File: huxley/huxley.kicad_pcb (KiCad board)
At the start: 4 copper layers, 104 parts, among them J1 SMA_RF2-04A-T-00-50-G, J10 SMA_RF2-04A-T-00-50-G, J11 SMA_RF2-04A-T-00-50-G, J12 SMA_RF2-04A-T-00-50-G, J13 SMA_RF2-04A-T-00-50-G, J14 SMA_RF2-04A-T-00-50-G, J15 SMA_RF2-04A-T-00-50-G, J16 SMA_RF2-04A-T-00-50-G, J17 SMA_RF2-04A-T-00-50-G, J18 SMA_RF2-04A-T-00-50-G, J19 SMA_RF2-04A-T-00-50-G, J2 SMA_RF2-04A-T-00-50-G, J20 SMA_RF2-04A-T-00-50-G, J21 61300211121, J22 SMA_RF2-04A-T-00-50-G, J23 SMA_RF2-04A-T-00-50-G, J24 SMA_RF2-04A-T-00-50-G, J25 61300211121, J26 61300211121, J27 61300211121, J28 61300211121, J29 61300211121, J3 SMA_RF2-04A-T-00-50-G, J30 61300211121, J31 61300211121, J32 61300211121, J33 67996-130HLF, J4 SMA_RF2-04A-T-00-50-G, J5 SMA_RF2-04A-T-00-50-G, J6 SMA_RF2-04A-T-00-50-G, J7 SMA_RF2-04A-T-00-50-G, J8 SMA_RF2-04A-T-00-50-G, J9 SMA_RF2-04A-T-00-50-G, U2 LM134H, U3 MAX40201FAUA+, U4 TMUX1112PWR, U5 TMUX1112PWR, U6 NVT2010PW_118

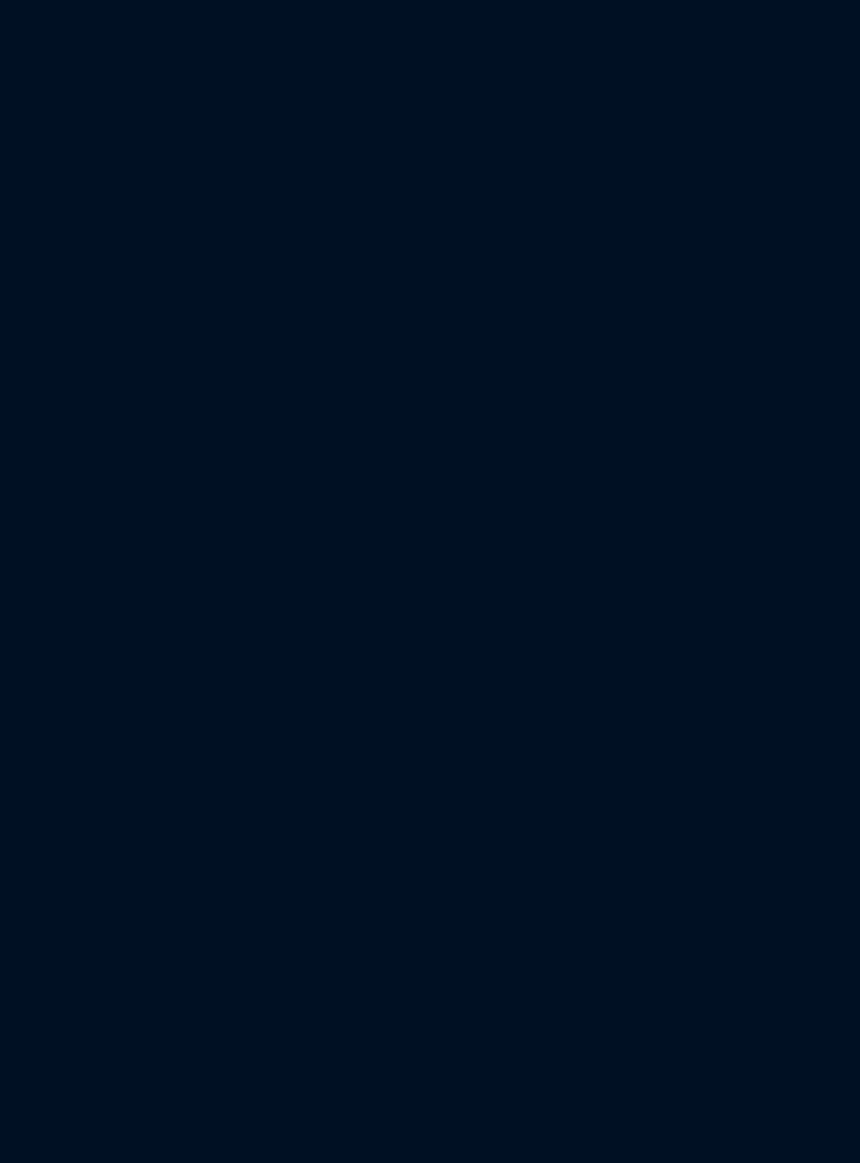
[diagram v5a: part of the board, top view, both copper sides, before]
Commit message: added banana plugs and fixed analog discovery pinout
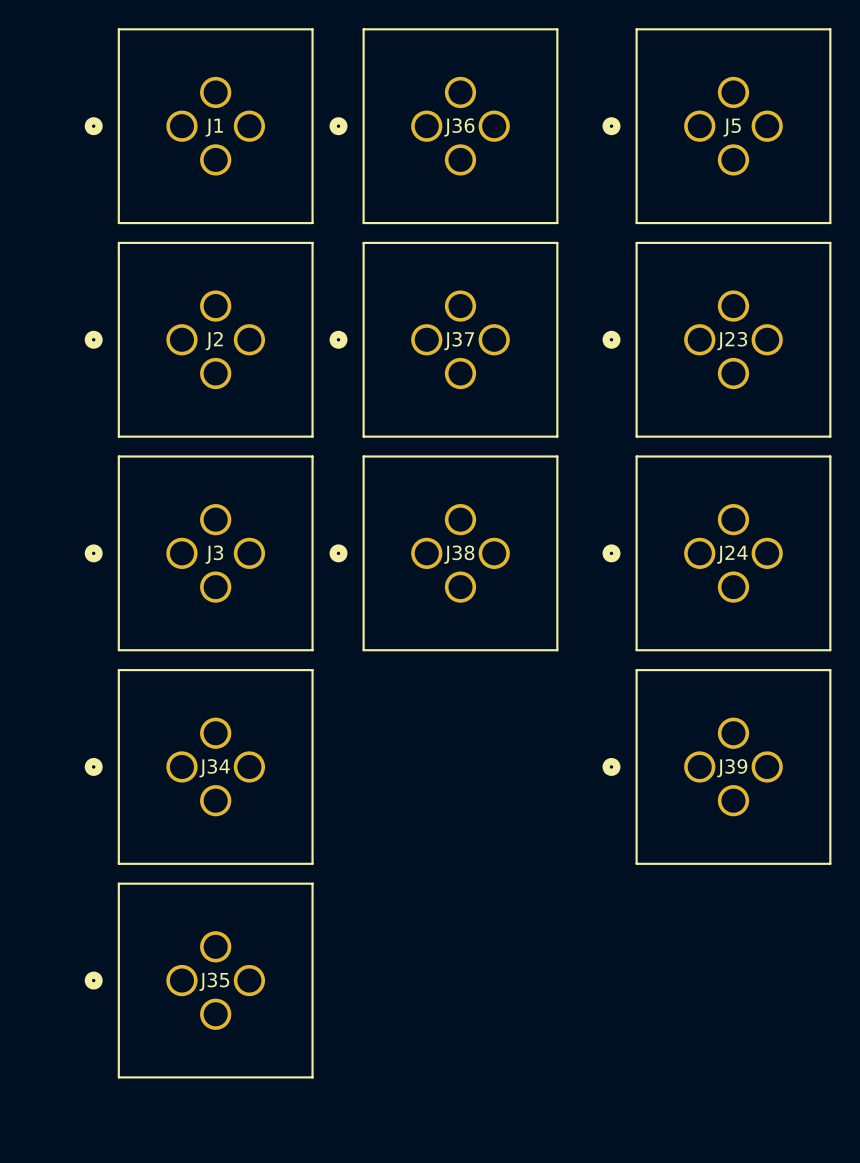
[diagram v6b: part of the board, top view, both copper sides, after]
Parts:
- added J1: CT3151V1-2, 726_footprints:banana_plug_CT3151V1-0, F.Cu at (193.6, 28.1)
- added J2: CT3151V1-2, 726_footprints:banana_plug_CT3151V1-0, F.Cu at (193.6, 43.3)
- added J23: CT3151V1-0, 726_footprints:banana_plug_CT3151V1-0, F.Cu at (230.2, 43.3)
- added J24: CT3151V1-2, 726_footprints:banana_plug_CT3151V1-0, F.Cu at (230.2, 58.4)
- added J3: CT3151V1-2, 726_footprints:banana_plug_CT3151V1-0, F.Cu at (193.6, 58.4)
- added J34: CT3151V1-0, 726_footprints:banana_plug_CT3151V1-0, F.Cu at (193.6, 73.5)
- added J35: CT3151V1-2, 726_footprints:banana_plug_CT3151V1-0, F.Cu at (193.6, 88.6)
- added J36: CT3151V1-0, 726_footprints:banana_plug_CT3151V1-0, F.Cu at (210.9, 28.1)
- added J37: CT3151V1-0, 726_footprints:banana_plug_CT3151V1-0, F.Cu at (210.9, 43.3)
- added J38: CT3151V1-0, 726_footprints:banana_plug_CT3151V1-0, F.Cu at (210.9, 58.4)
- added J39: CT3151V1-2, 726_footprints:banana_plug_CT3151V1-0, F.Cu at (230.2, 73.5)
- added J5: CT3151V1-0, 726_footprints:banana_plug_CT3151V1-0, F.Cu at (230.2, 28.1)
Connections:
- C16 pad 1: PP_TAVDD_1V8 -> +3.3V
- C17 pad 1: PP_TAVDD_1V8 -> +3.3V
- J33 pad 1: unconnected-(J33-Pad1) -> SPI_CS_L_3V3
- J33 pad 10: SPI_COPI_3V3 -> IBIAS_SEL1
- J33 pad 11: RST_L_3V3 -> IBIAS_SEL2
- J33 pad 12: SCAN_EN_3V3 -> IBIAS_SEL3
- J33 pad 13: unconnected-(J33-Pad13) -> IBIAS_SEL4
- J33 pad 19: unconnected-(J33-Pad19) -> GND
- J33 pad 2: unconnected-(J33-Pad2) -> SPI_CLK_3V3
- J33 pad 20: unconnected-(J33-Pad20) -> GND
- J33 pad 23: IBIAS_SEL1 -> unconnected-(J33-Pad23)
- J33 pad 24: IBIAS_SEL2 -> unconnected-(J33-Pad24)
- J33 pad 25: IBIAS_SEL3 -> GND
- J33 pad 26: IBIAS_SEL4 -> GND
- J33 pad 27: TSCAN_EN_3V3 -> unconnected-(J33-Pad27)
- J33 pad 28: IO_UCLK_3V3 -> unconnected-(J33-Pad28)
- J33 pad 29: SPI_CIPO_3V3 -> unconnected-(J33-Pad29)
- J33 pad 3: unconnected-(J33-Pad3) -> SPI_COPI_3V3
- J33 pad 30: TSCAN_OUT_3V3 -> unconnected-(J33-Pad30)
- J33 pad 4: unconnected-(J33-Pad4) -> RST_L_3V3
- J33 pad 5: unconnected-(J33-Pad5) -> SCAN_EN_3V3
- J33 pad 6: unconnected-(J33-Pad6) -> TSCAN_EN_3V3
- J33 pad 7: unconnected-(J33-Pad7) -> IO_UCLK_3V3
- J33 pad 8: SPI_CS_L_3V3 -> SPI_CIPO_3V3
- J33 pad 9: SPI_CLK_3V3 -> TSCAN_OUT_3V3
- U4 pad 13: PP_TAVDD_1V8 -> +3.3V

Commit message: layout_1003
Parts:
- removed the J1 at (58.9, 119.6)
- removed J10, J12, J14, J16, J23, J6, J8: SMA_RF2-04A-T-00-50-G, 726_footprints:CONN_RF2-04A-T-00-50-G_ADM
- removed the J2 at (138.8, 121.8)
- removed the J24 at (116.3, 59.1)
- removed the J3 at (38.3, 43.4)
- removed the J34 at (193.6, 73.5)
- removed J36, J38: CT3151V1-0, 726_footprints:banana_plug_CT3151V1-0
- removed the J37 at (210.9, 43.3)
- C13, C14, C15, C16, C17, C18, C19, C20, C21, C22, C23, C24, C25, C26, C27, C28, C29, C30, C31, C32, C33, C34, C35, C36, C37, C38, C39, C40, C41, C42, C43: footprint Capacitor_SMD:C_0402_1005Metric -> Capacitor_SMD:C_0603_1608Metric
- R1, R10, R11, R12, R2, R3, R4, R5, R6, R7, R8, R9: footprint Resistor_SMD:R_2512_6332Metric -> Resistor_SMD:R_0603_1608Metric
- moved J37 219.4 mm to (36.7, 146.7)
- moved J34 196.1 mm to (35.0, 46.6)
- moved J3 163.8 mm to (55.7, 146.8)
- moved J2 161.4 mm to (35.7, 77.1)
- moved J24 150.8 mm to (79.9, 46.3)
- moved J35 144.4 mm to (55.5, 46.4)
- moved J1 122.5 mm to (152.7, 143.6)
- moved J5 90.6 mm to (92.2, 145.3)
- moved J39 82.3 mm to (148.0, 70.2)
- moved C43 57.6 mm to (93.5, 76.7)
- moved C42 57.0 mm to (93.5, 73.7)
- moved C41 56.5 mm to (93.5, 70.7)
- moved C40 56.1 mm to (93.5, 67.9)
- moved J17 42.9 mm to (138.4, 88.9)
- moved C39 42.4 mm to (122.7, 76.7), turned to 180 degrees
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- renumbered J5 to J34, J23 to J37
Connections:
- C18 pad 1: PP_TAVDD_1V8 -> +3.3V
- C19 pad 1: PP_TAVDD_1V8 -> +3.3V
- J11 pad 2: GND -> output_3b
- J11 pad 3: GND -> output_3b
- J11 pad 4: GND -> output_3b
- J11 pad 5: GND -> output_3b
- J13 pad 2: GND -> output_4b
- J13 pad 3: GND -> output_4b
- J13 pad 4: GND -> output_4b
- J13 pad 5: GND -> output_4b
- J15 pad 2: GND -> output_5b
- J15 pad 3: GND -> output_5b
- J15 pad 4: GND -> output_5b
- J15 pad 5: GND -> output_5b
- J4 pad 2: GND -> output_0b
- J4 pad 3: GND -> output_0b
- J4 pad 4: GND -> output_0b
- J4 pad 5: GND -> output_0b
- J5 pad 1: PP_TAVDD_1V8 -> CLK
- J7 pad 2: GND -> output_1b
- J7 pad 3: GND -> output_1b
- J7 pad 4: GND -> output_1b
- J7 pad 5: GND -> output_1b
- J9 pad 2: GND -> output_2b
- J9 pad 3: GND -> output_2b
- J9 pad 4: GND -> output_2b
- J9 pad 5: GND -> output_2b
- U5 pad 13: PP_TAVDD_1V8 -> +3.3V
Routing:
- net IBIAS_SEL1: track 0.00 -> 236.5 mm, vias 0 -> 3
- net IBIAS_SEL3: track 0.00 -> 225.4 mm, vias 0 -> 2
- net IBIAS_SEL4: track 0.00 -> 218.2 mm, vias 0 -> 2
- net IBIAS_SEL2: track 0.00 -> 215.9 mm, vias 0 -> 3
- net /ibias/ibias_rset: track 0.20 -> 201.8 mm, vias 0 -> 2
- net iout_dummy: track 0.00 -> 75.4 mm
- net GND: track 3.15 -> 69.6 mm, vias 59 -> 65
- net output_2b: track 0.00 -> 56.2 mm
- net PP_TAVDD_1V8: track 58.9 -> 4.51 mm, vias 0 -> 4
- net output_5b: track 0.00 -> 53.7 mm
- net IO_UCLK: track 0.00 -> 53.6 mm
- net Net-(D1-A): track 1.74 -> 54.4 mm
- net output_1b: track 0.00 -> 52.4 mm
- net output_0b: track 0.00 -> 51.9 mm
- net TSCAN_OUT: track 0.00 -> 48.9 mm
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- added copper zone on In2.Cu, net +3.3V
- added copper zone on B.Cu, net vbias1
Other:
- board outline added: 150 x 150 mm
- board text added: "Designator1018"
- board text added: "output_0"
- board text added: "output_1"
- board text added: "output_2"
- board text added: "output_3"
- board text added: "output_4"
- board text added: "output_5"
- board text removed: "output_2a"
- board text removed: "output_2b"

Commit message: layout_1003_1
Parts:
- U4, U5: footprint 726_footprints:TMUX1111PWR -> Package_SO:TSSOP-16_4.4x5mm_P0.65mm
- moved J3 2.06 mm to (57.7, 146.6)
- moved J22 0.80 mm to (39.6, 62.2)
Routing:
- net IBIAS_SEL2: track 215.9 -> 223.7 mm
- net IBIAS_SEL4: track 218.2 -> 224.6 mm
- net IBIAS_SEL3: track 225.4 -> 230.0 mm
- net /ibias/ibias_rset: track 201.8 -> 206.1 mm
- net IBIAS_SEL1: track 236.5 -> 239.9 mm
- net iout_dummy_amp: track 24.4 -> 25.7 mm
- net Net-(D1-A): track 54.4 -> 53.4 mm
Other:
- board text added: "3.3V"
- board text added: "CLK"
- board text added: "GND"
- board text added: "PP_TAVDD_1V8"
- board text added: "PP_VDDIO_1V8"
- board text added: "PP_VDD_0V9"
- board text added: "R1_1"
- board text added: "R1_2"
- board text added: "R1_3"
- board text added: "R1_4"
- board text added: "R2_1"
- board text added: "R2_2"
- board text added: "R2_3"
- board text added: "R2_4"
- board text added: "iout_dummy"
- board text added: "iout_dummy_amp"
- board text added: "vbias0"
- board text added: "vbias1"
- board text added: "vbias2"
- board text added: "vd1_dummy"
- board text added: "vlvl"
- board text added: "vlvl_p_dummy"
- board text added: "vrbias"
